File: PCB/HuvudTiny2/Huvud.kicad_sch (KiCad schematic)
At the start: 99 parts, among them J1 Vin, J12 USB_Micro-B, J2 DBG, J3 THERM, J4 FAN0, J5 FAN1, J6 Heater, J7 Endstop, J9 STEPPER, Q1 AO3400A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

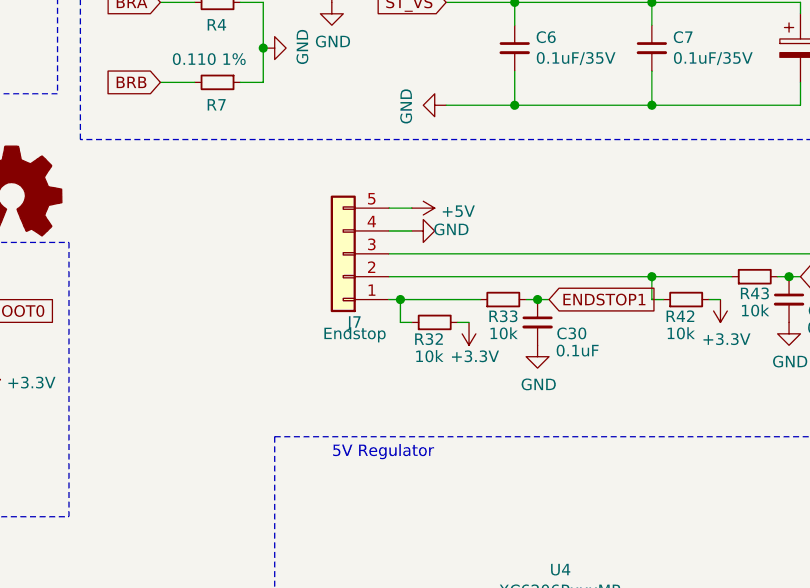
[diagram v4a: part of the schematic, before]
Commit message: Add protection diode on endstop 1. Add back heatsink for power mosfet.
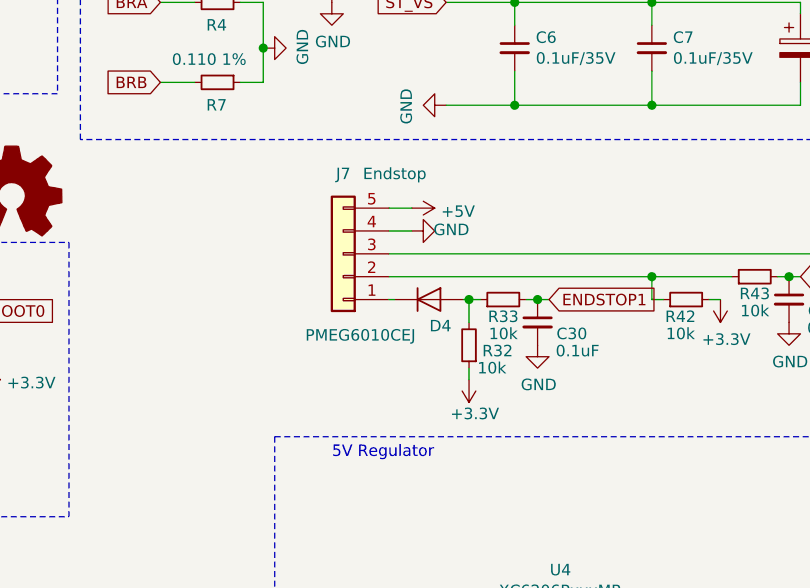
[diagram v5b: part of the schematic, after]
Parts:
- added D4: PMEG6010CEJ, Diode_SMD:D_SOD-323F, symbol Device:D
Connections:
- net +3V3: now also R32.1; no longer R32.2
- new net: D4.1 (K), J7.1 (Pin_1)
- new net: D4.2 (A), R32.2, R33.1
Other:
- moved on the sheet: R32
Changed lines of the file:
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@@
   (junction (at 184.15 66.04) (diameter 1.016) (color 0 0 0 0))
   (junction (at 184.15 69.85) (diameter 1.016) (color 0 0 0 0))
-  (junction (at 191.77 109.22) (diameter 1.016) (color 0 0 0 0))
+  (junction (at 199.39 109.22) (diameter 1.016) (color 0 0 0 0))
   (junction (at 200.66 145.415) (diameter 1.016) (color 0 0 0 0))
   (junction (at 204.47 76.2) (diameter 1.016) (color 0 0 0 0))
@@
     (stroke (width 0) (type solid) (color 0 0 0 0))
   )
-  (wire (pts (xy 190.5 109.22) (xy 191.77 109.22))
+  (wire (pts (xy 190.5 109.22) (xy 191.135 109.22))
     (stroke (width 0) (type solid) (color 0 0 0 0))
   )
@@
     (stroke (width 0) (type solid) (color 0 0 0 0))
   )
-  (wire (pts (xy 191.77 109.22) (xy 200.66 109.22))
+  (wire (pts (xy 193.04 99.06) (xy 190.5 99.06))
     (stroke (width 0) (type solid) (color 0 0 0 0))
   )
-  (wire (pts (xy 191.77 111.76) (xy 191.77 109.22))
+  (wire (pts (xy 193.04 101.6) (xy 190.5 101.6))
     (stroke (width 0) (type solid) (color 0 0 0 0))
   )
-  (wire (pts (xy 193.04 99.06) (xy 190.5 99.06))
+  (wire (pts (xy 196.85 76.2) (xy 204.47 76.2))
     (stroke (width 0) (type solid) (color 0 0 0 0))
   )
-  (wire (pts (xy 193.04 101.6) (xy 190.5 101.6))
+  (wire (pts (xy 196.85 87.63) (xy 204.47 87.63))
     (stroke (width 0) (type solid) (color 0 0 0 0))
   )
-  (wire (pts (xy 193.04 111.76) (xy 191.77 111.76))
+  (wire (pts (xy 198.755 109.22) (xy 199.39 109.22))
     (stroke (width 0) (type solid) (color 0 0 0 0))
   )
-  (wire (pts (xy 196.85 76.2) (xy 204.47 76.2))
+  (wire (pts (xy 199.39 109.22) (xy 199.39 111.76))
     (stroke (width 0) (type solid) (color 0 0 0 0))
   )
-  (wire (pts (xy 196.85 87.63) (xy 204.47 87.63))
+  (wire (pts (xy 199.39 109.22) (xy 200.66 109.22))
     (stroke (width 0) (type solid) (color 0 0 0 0))
   )
-  (wire (pts (xy 198.12 111.76) (xy 199.39 111.76))
+  (wire (pts (xy 199.39 116.84) (xy 199.39 118.11))
     (stroke (width 0) (type solid) (color 0 0 0 0))
   )
@@
     (pin "1")
   )
-  (symbol (lib_id "power:+3.3V") (at 199.39 111.76 180) (unit 1)
+  (symbol (lib_id "power:+3.3V") (at 199.39 118.11 180) (unit 1)
     (in_bom yes) (on_board yes)
-    (property "Reference" "#PWR050" (id 0) (at 199.39 107.95 0)
+    (property "Reference" "#PWR050" (id 0) (at 199.39 114.3 0)
       (effects (font (size 1.27 1.27)) hide)
     )
-    (property "Value" "+3.3V" (id 1) (at 200.025 115.57 0))
-    (property "Footprint" "" (id 2) (at 199.39 111.76 0)
+    (property "Value" "+3.3V" (id 1) (at 200.025 121.92 0))
+    (property "Footprint" "" (id 2) (at 199.39 118.11 0)
       (effects (font (size 1.27 1.27)) hide)
     )
-    (property "Datasheet" "" (id 3) (at 199.39 111.76 0)
+    (property "Datasheet" "" (id 3) (at 199.39 118.11 0)
       (effects (font (size 1.27 1.27)) hide)
     )
@@
     (pin "2")
   )
-  (symbol (lib_id "Device:R_Small") (at 195.58 111.76 90) (unit 1)
+  (symbol (lib_id "Device:R_Small") (at 199.39 114.3 180) (unit 1)
     (in_bom yes) (on_board yes)
-    (property "Reference" "R32" (id 0) (at 194.945 113.665 90))
-    (property "Value" "10k" (id 1) (at 194.945 115.57 90))
-    (property "Footprint" "Resistor_SMD:R_0402_1005Metric" (id 2) (at 195.58 111.76 0)
+    (property "Reference" "R32" (id 0) (at 202.565 114.935 0))
+    (property "Value" "10k" (id 1) (at 201.93 116.84 0))
+    (property "Footprint" "Resistor_SMD:R_0402_1005Metric" (id 2) (at 199.39 114.3 0)
       (effects (font (size 1.27 1.27)) hide)
     )
-    (property "Datasheet" "~" (id 3) (at 195.58 111.76 0)
+    (property "Datasheet" "~" (id 3) (at 199.39 114.3 0)
       (effects (font (size 1.27 1.27)) hide)
     )
-    (property "LCSC" "C25744" (id 4) (at 195.58 111.76 0)
+    (property "LCSC" "C25744" (id 4) (at 199.39 114.3 0)
       (effects (font (size 1.27 1.27)) hide)
     )
@@
     (pin "1")
   )
+  (symbol (lib_id "Device:D") (at 194.945 109.22 0) (unit 1)
+    (in_bom yes) (on_board yes)
+    (property "Reference" "D4" (id 0) (at 196.215 112.1622 0))
+    (property "Value" "PMEG6010CEJ" (id 1) (at 187.325 113.1909 0))
+    (property "Footprint" "Diode_SMD:D_SOD-323F" (id 2) (at 194.945 109.22 0)
+      (effects (font (size 1.27 1.27)) hide)
+    )
+    (property "Datasheet" "~" (id 3) (at 194.945 109.22 0)
+      (effects (font (size 1.27 1.27)) hide)
+    )
+    (property "LCSC" "C406049" (id 4) (at 194.945 109.22 0)
+      (effects (font (size 1.27 1.27)) hide)
+    )
+    (pin "1")
+    (pin "2")
+  )
   (symbol (lib_id "Mechanical:MountingHole_Pad") (at 121.92 90.17 0) (unit 1)
     (in_bom yes) (on_board yes)
@@
   (symbol (lib_id "Connector_Generic:Conn_01x05") (at 185.42 104.14 180) (unit 1)
     (in_bom yes) (on_board yes)
-    (property "Reference" "J7" (id 0) (at 186.69 111.76 0))
-    (property "Value" "Endstop" (id 1) (at 186.69 113.03 0))
+    (property "Reference" "J7" (id 0) (at 185.42 95.25 0))
+    (property "Value" "Endstop" (id 1) (at 191.135 95.25 0))
     (property "Footprint" "Connector_JST:JST_PH_B5B-PH-K_1x05_P2.00mm_Vertical" (id 2) (at 185.42 104.14 0)
       (effects (font (size 1.27 1.27)) hide)
@@
       (reference "D3") (unit 1) (value "LEDGR") (footprint "LED_SMD:LED_0402_1005Metric")
     )
+    (path "/f2a074ca-d90f-4884-81b5-731a56fa8dd9"
+      (reference "D4") (unit 1) (value "PMEG6010CEJ") (footprint "Diode_SMD:D_SOD-323F")
+    )
     (path "/00000000-0000-0000-0000-0000601abab2"

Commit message: Update sense resistors to 0.1 1206 size.
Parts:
- R4, R7: value 0.110 1% -> 0.1 1%; footprint Resistor_SMD:R_0805_2012Metric -> Resistor_SMD:R_1206_3216Metric; LCSC C53899 -> C25334
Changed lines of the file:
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@@
       (effects (font (size 1.27 1.27)) (justify left))
     )
-    (property "Value" "0.110 1%" (id 1) (at 166.37 73.66 90)
-      (effects (font (size 1.27 1.27)) (justify left))
-    )
-    (property "Footprint" "Resistor_SMD:R_0805_2012Metric" (id 2) (at 171.45 76.2 0)
+    (property "Value" "0.1 1%" (id 1) (at 166.37 73.66 90)
+      (effects (font (size 1.27 1.27)) (justify left))
+    )
+    (property "Footprint" "Resistor_SMD:R_1206_3216Metric" (id 2) (at 171.45 76.2 0)
       (effects (font (size 1.27 1.27)) hide)
     )
@@
       (effects (font (size 1.27 1.27)) hide)
     )
-    (property "LCSC" "C53899" (id 4) (at 171.45 76.2 0)
+    (property "LCSC" "C25334" (id 4) (at 171.45 76.2 0)
       (effects (font (size 1.27 1.27)) hide)
     )
@@
       (effects (font (size 1.27 1.27)) (justify left))
     )
-    (property "Value" "0.110 1%" (id 1) (at 166.37 82.55 90)
-      (effects (font (size 1.27 1.27)) (justify left))
-    )
-    (property "Footprint" "Resistor_SMD:R_0805_2012Metric" (id 2) (at 171.45 85.09 0)
+    (property "Value" "0.1 1%" (id 1) (at 166.37 82.55 90)
+      (effects (font (size 1.27 1.27)) (justify left))
+    )
+    (property "Footprint" "Resistor_SMD:R_1206_3216Metric" (id 2) (at 171.45 85.09 0)
       (effects (font (size 1.27 1.27)) hide)
     )
@@
       (effects (font (size 1.27 1.27)) hide)
     )
-    (property "LCSC" "C53899" (id 4) (at 171.45 85.09 0)
+    (property "LCSC" "C25334" (id 4) (at 171.45 85.09 0)
       (effects (font (size 1.27 1.27)) hide)
     )
@@
     )
     (path "/00000000-0000-0000-0000-00005ecd2559"
-      (reference "R4") (unit 1) (value "0.110 1%") (footprint "Resistor_SMD:R_0805_2012Metric")
+      (reference "R4") (unit 1) (value "0.1 1%") (footprint "Resistor_SMD:R_1206_3216Metric")
     )
     (path "/00000000-0000-0000-0000-00005e85b70d"
@@
     )
     (path "/00000000-0000-0000-0000-00005ecd2b5c"
-      (reference "R7") (unit 1) (value "0.110 1%") (footprint "Resistor_SMD:R_0805_2012Metric")
+      (reference "R7") (unit 1) (value "0.1 1%") (footprint "Resistor_SMD:R_1206_3216Metric")
     )
     (path "/00000000-0000-0000-0000-00005e8a8f7a"

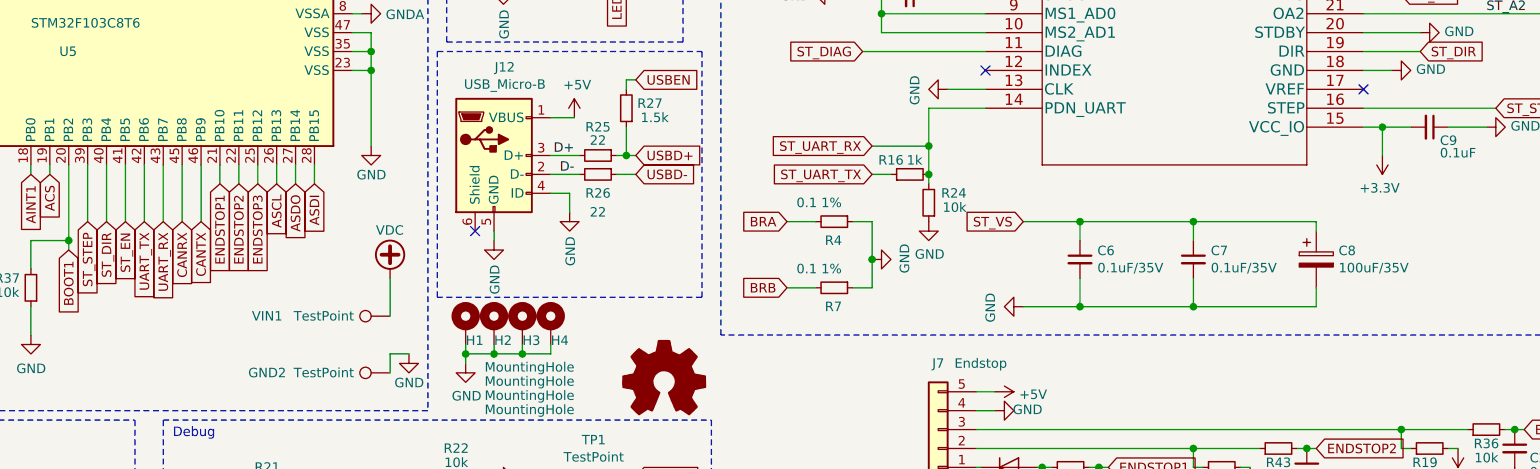
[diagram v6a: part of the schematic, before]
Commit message: Route VCC_IO to GPIO pin so we can reset the stepper driver.
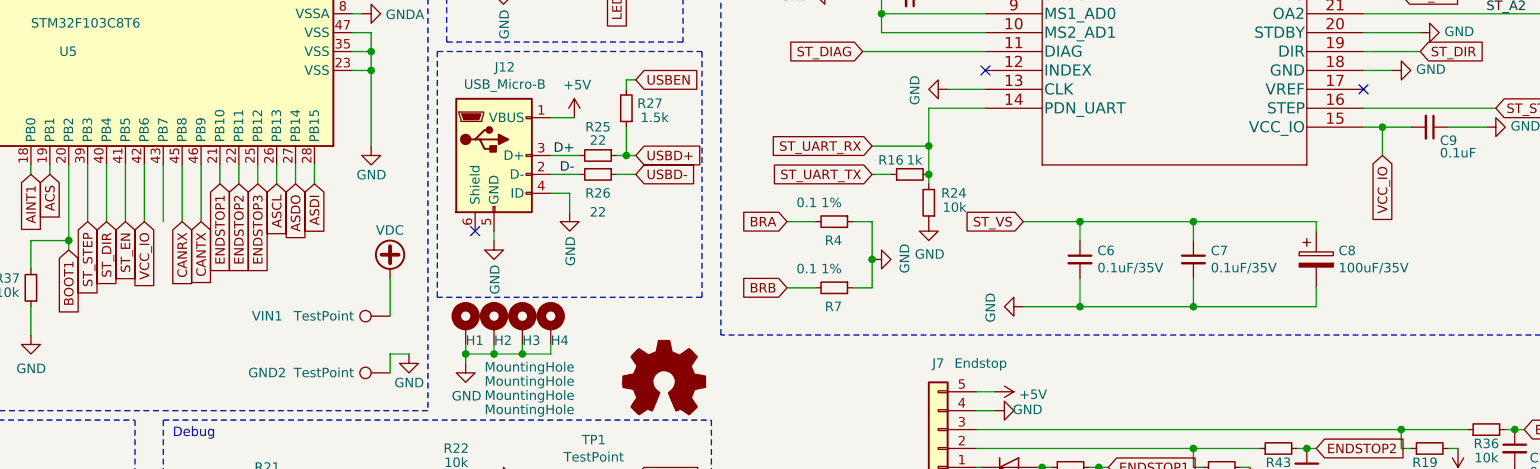
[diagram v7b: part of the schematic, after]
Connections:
- net +3V3: no longer C9.2, U2.15 (VCC_IO)
- net UART_RX: no longer names the net of U5.43 (PB7)
- net UART_TX renamed VCC_IO
- net VCC_IO: now also C9.2, U2.15 (VCC_IO)
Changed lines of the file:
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@@
     )
   )
-  (global_label "UART_TX" (shape input) (at 78.74 76.2 270) (fields_autoplaced)
+  (global_label "VCC_IO" (shape input) (at 78.74 76.2 270) (fields_autoplaced)
     (effects (font (size 1.27 1.27)) (justify right))
-    (property "Intersheet References" "${INTERSHEET_REFS}" (id 0) (at 0 0 0)
-      (effects (font (size 1.27 1.27)) hide)
+    (property "Intersheet References" "${INTERSHEET_REFS}" (id 0) (at 78.6606 85.1445 90)
+      (effects (font (size 1.27 1.27)) (justify right) hide)
     )
   )
@@
     )
   )
-  (global_label "UART_RX" (shape input) (at 81.28 76.2 270) (fields_autoplaced)
-    (effects (font (size 1.27 1.27)) (justify right))
-    (property "Intersheet References" "${INTERSHEET_REFS}" (id 0) (at 0 0 0)
-      (effects (font (size 1.27 1.27)) hide)
-    )
-  )
   (global_label "FAN0" (shape input) (at 83.82 30.48 90) (fields_autoplaced)
     (effects (font (size 1.27 1.27)) (justify left))
@@
     )
   )
+  (global_label "VCC_IO" (shape input) (at 245.11 67.31 270) (fields_autoplaced)
+    (effects (font (size 1.27 1.27)) (justify right))
+    (property "Intersheet References" "${INTERSHEET_REFS}" (id 0) (at 245.0306 76.2545 90)
+      (effects (font (size 1.27 1.27)) (justify right) hide)
+    )
+  )
   (global_label "ST_VS" (shape input) (at 247.65 30.48 0) (fields_autoplaced)
     (effects (font (size 1.27 1.27)) (justify left))
@@
     (pin "1")
   )
-  (symbol (lib_id "power:+3.3V") (at 245.11 67.31 180) (unit 1)
-    (in_bom yes) (on_board yes)
-    (property "Reference" "#PWR0103" (id 0) (at 245.11 63.5 0)
-      (effects (font (size 1.27 1.27)) hide)
-    )
-    (property "Value" "+3.3V" (id 1) (at 244.729 71.7042 0))
-    (property "Footprint" "" (id 2) (at 245.11 67.31 0)
-      (effects (font (size 1.27 1.27)) hide)
-    )
-    (property "Datasheet" "" (id 3) (at 245.11 67.31 0)
-      (effects (font (size 1.27 1.27)) hide)
-    )
-    (pin "1")
-  )
   (symbol (lib_id "power:+3.3V") (at 255.27 106.68 180) (unit 1)
     (in_bom yes) (on_board yes)
@@
       (reference "#PWR0102") (unit 1) (value "GND") (footprint "")
     )
-    (path "/00000000-0000-0000-0000-00005f8c9094"
-      (reference "#PWR0103") (unit 1) (value "+3.3V") (footprint "")
-    )
     (path "/00000000-0000-0000-0000-00005ef3d573"

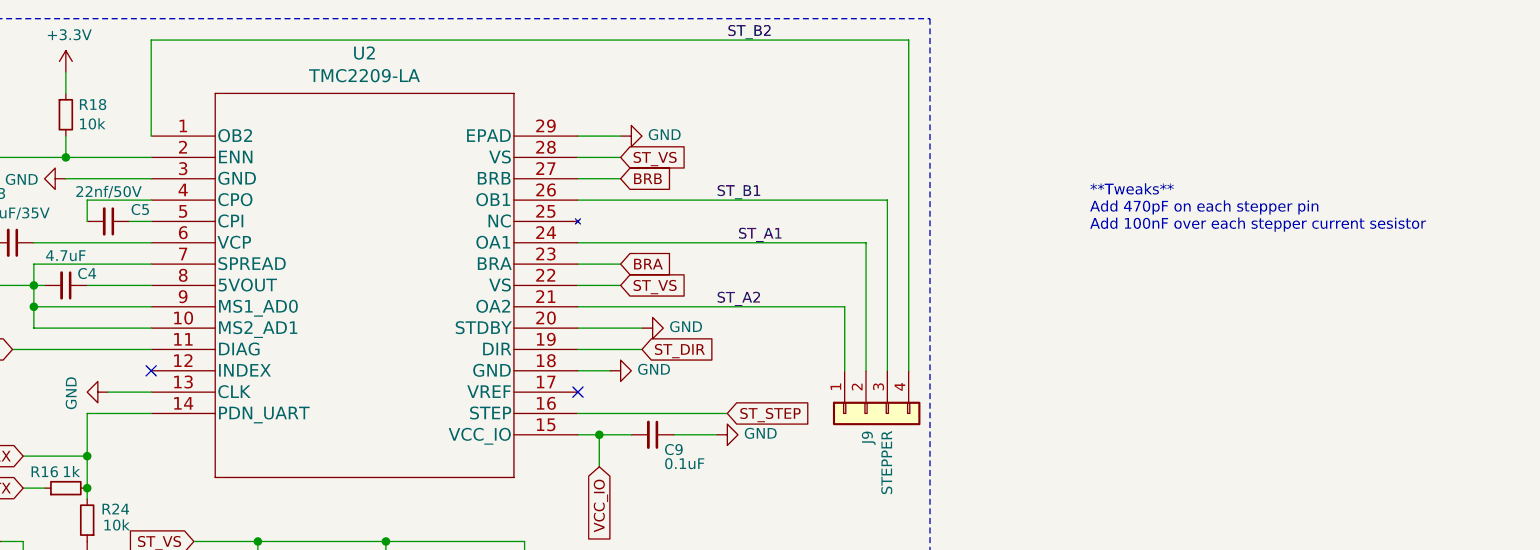
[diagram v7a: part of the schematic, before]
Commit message: Added caps across stepper pins.
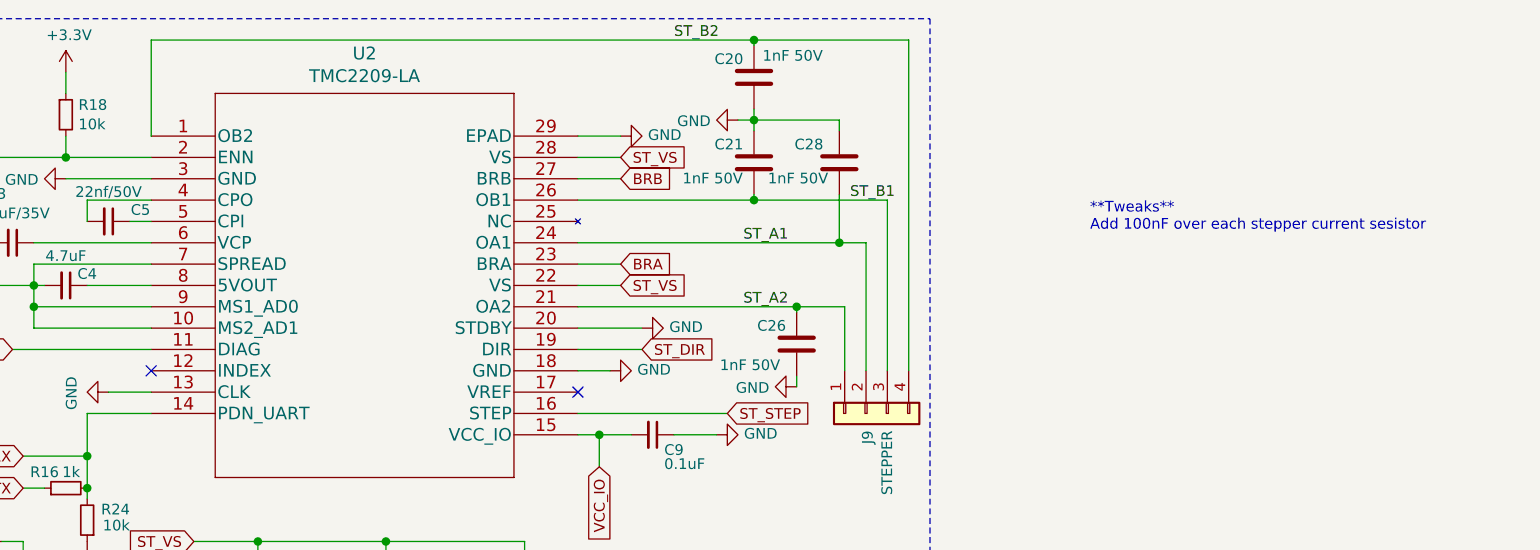
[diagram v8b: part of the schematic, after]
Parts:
- added C20, C21, C26, C28: 1nF 50V, Capacitor_SMD:C_0402_1005Metric, symbol Device:C
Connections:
- net GND: now also C20.2, C21.1, C26.2, C28.1
- net ST_A1: now also C28.2
- net ST_A2: now also C26.1
- net ST_B1: now also C21.2
- net ST_B2: now also C20.1
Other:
- note added: "**Tweaks** Add 100nF over each stepper current sesistor"
- note removed: "**Tweaks** Add 470pF on each stepper pin Add 100nF over each stepper current sesistor"
